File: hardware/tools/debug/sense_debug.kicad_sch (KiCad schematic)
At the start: 54 parts, among them J1 Conn_01x03_Pin, J2 Conn_01x20_Pin, J3 Conn_01x03_Pin, J4 Conn_01x15_Pin, J5 Conn_01x12_Pin, J6 B2B-PH-SM4-TB_LF__SN_, J7 Conn_01x03_Pin, Q1 Si1308EDL, U1 TMP117AIDRVR, U2 NTAG link, U3 ATtiny1626-MFR

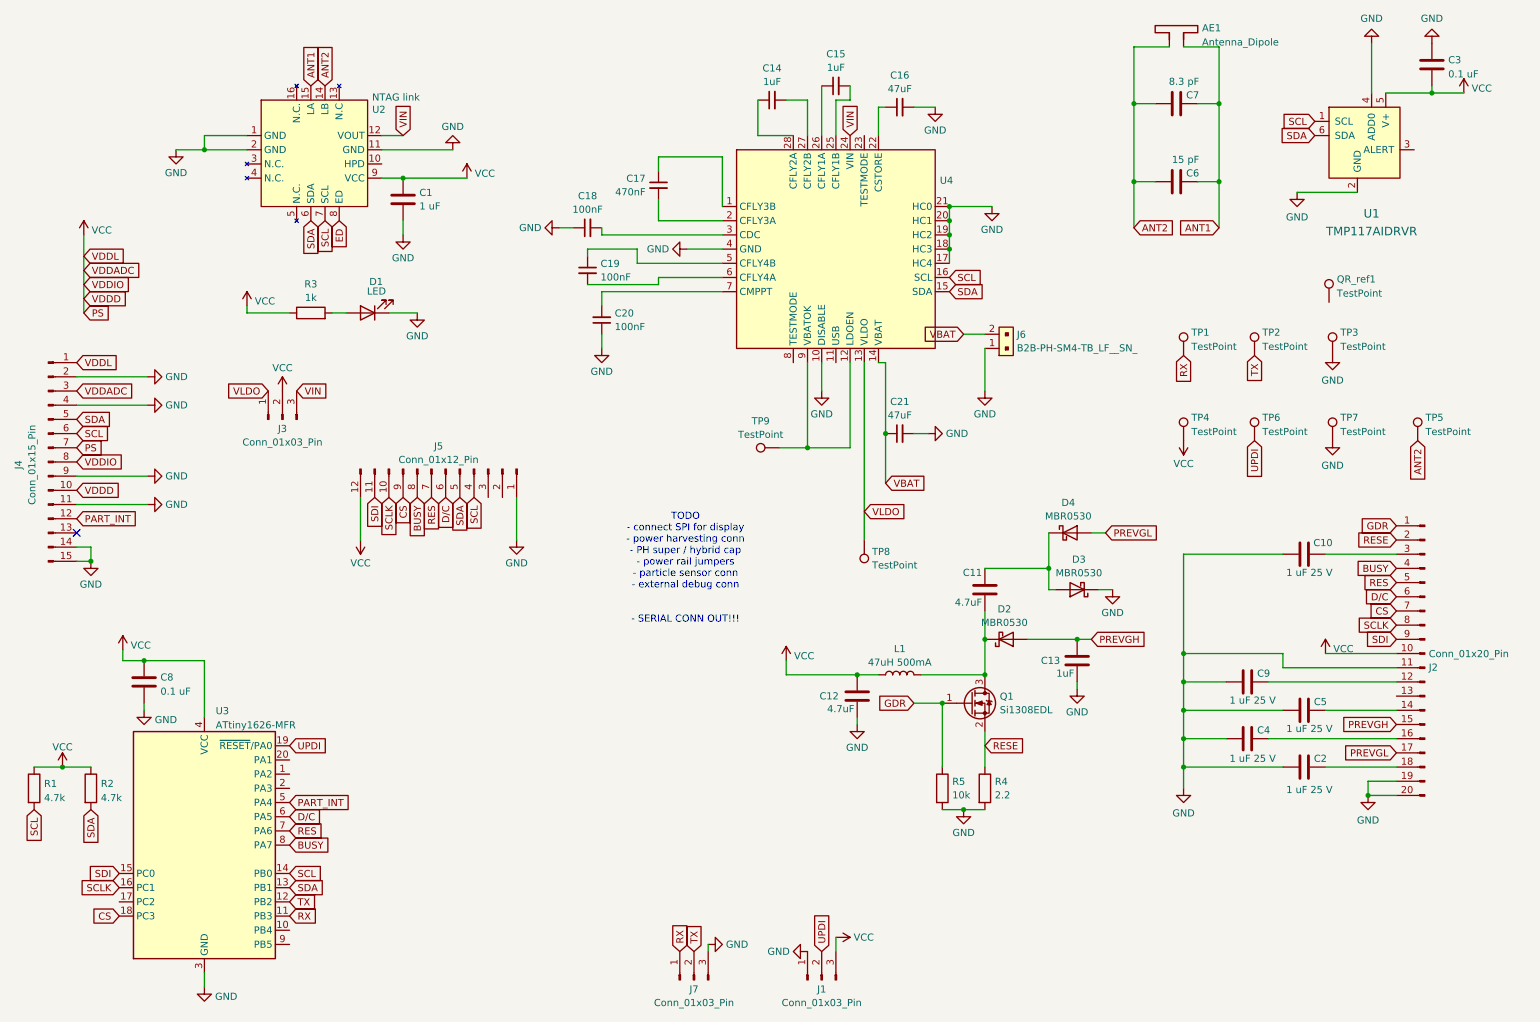
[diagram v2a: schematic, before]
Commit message: new screen debug board
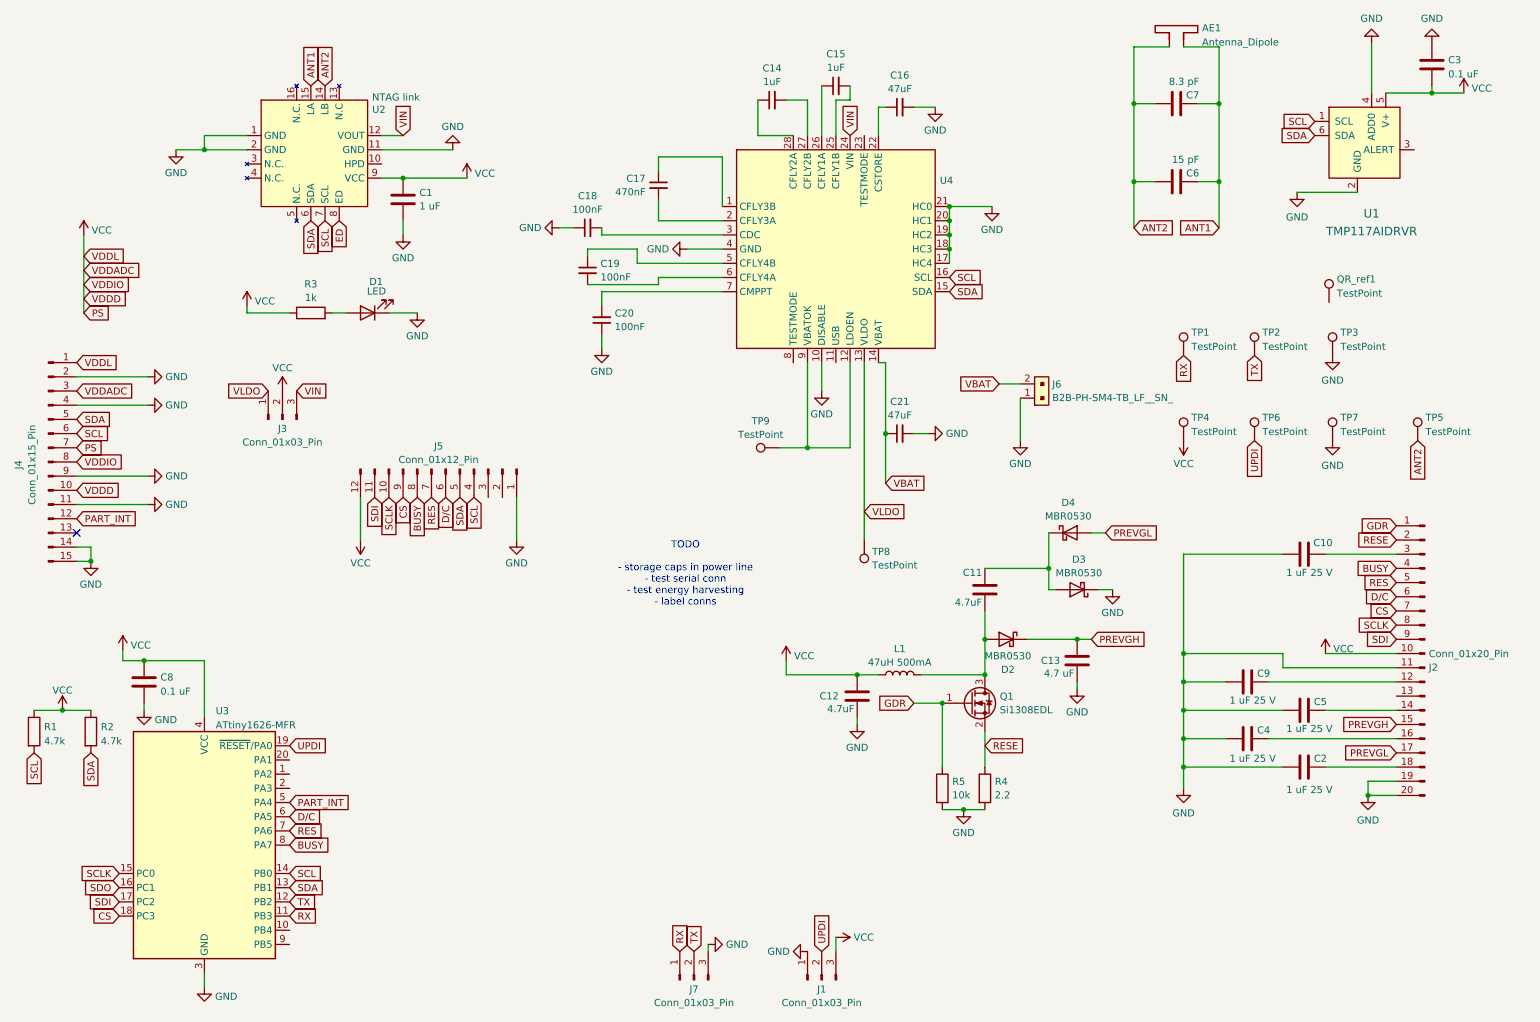
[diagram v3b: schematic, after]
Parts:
- C13: value 1uF -> 4.7 uF
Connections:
- net PREVGH: now also D2.1 (K); no longer D2.2 (A)
- net SCLK: now also U3.15 (PC0); no longer U3.16 (PC1)
- net SDI: now also U3.17 (PC2); no longer U3.15 (PC0)
- net at C11.1, L1.2, Q1.3 (D): now also D2.2 (A); no longer D2.1 (K)
- new net SDO: U3.16 (PC1)
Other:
- note added: "TODO - storage caps in power line - test serial conn - test energy harvesting - label conns"
- note removed: "TODO - connect SPI for display - power harvesting conn - PH super / hybrid cap - power rail jumpers - particle sensor conn - external debug conn - SERIAL CONN OUT!!!"
- moved on the sheet: J6, R1, R2
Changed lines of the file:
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@@
 	)
 	(junction
-		(at 22.86 149.86)
+		(at 22.86 139.7)
 		(diameter 0)
 		(color 0 0 0 0)
@@
 	(wire
 		(pts
-			(xy 17.78 149.86) (xy 22.86 149.86)
+			(xy 17.78 139.7) (xy 22.86 139.7)
 		)
 		(stroke
@@
 	(wire
 		(pts
-			(xy 184.15 72.39) (xy 187.96 72.39)
+			(xy 190.5 81.28) (xy 194.31 81.28)
 		)
 		(stroke
@@
 	(wire
 		(pts
-			(xy 22.86 149.86) (xy 27.94 149.86)
+			(xy 22.86 139.7) (xy 27.94 139.7)
 		)
 		(stroke
@@
 	(wire
 		(pts
-			(xy 187.96 74.93) (xy 187.96 82.55)
+			(xy 194.31 83.82) (xy 194.31 91.44)
 		)
 		(stroke
@@
 		)
 	)
-	(text "TODO\n- connect SPI for display\n- power harvesting conn\n- PH super / hybrid cap\n- power rail jumpers\n- particle sensor conn\n- external debug conn\n\n\n- SERIAL CONN OUT!!!\n\n"
+	(text "TODO\n\n- storage caps in power line\n- test serial conn\n- test energy harvesting\n- label conns"
 		(exclude_from_sim no)
 		(at 134.366 115.316 0)
@@
 	(global_label "VBAT"
 		(shape input)
-		(at 184.15 72.39 180)
+		(at 190.5 81.28 180)
 		(fields_autoplaced yes)
 		(effects
@@
 		)
 		(property "Intersheetrefs" "${INTERSHEET_REFS}"
-			(at 176.75 72.39 0)
+			(at 183.1 81.28 0)
 			(effects
 				(font
@@
 	(global_label "SDI"
 		(shape input)
-		(at 33.02 168.91 180)
+		(at 33.02 173.99 180)
 		(fields_autoplaced yes)
 		(effects
@@
 		)
 		(property "Intersheetrefs" "${INTERSHEET_REFS}"
-			(at 26.9505 168.91 0)
+			(at 26.9505 173.99 0)
 			(effects
 				(font
@@
 	(global_label "SDA"
 		(shape input)
-		(at 27.94 157.48 270)
+		(at 27.94 147.32 270)
 		(fields_autoplaced yes)
 		(effects
@@
 		)
 		(property "Intersheetrefs" "${INTERSHEET_REFS}"
-			(at 28.0194 163.4612 90)
+			(at 28.0194 153.3012 90)
 			(effects
 				(font
@@
 	(global_label "SCLK"
 		(shape input)
-		(at 33.02 171.45 180)
+		(at 33.02 168.91 180)
 		(fields_autoplaced yes)
 		(effects
@@
 		)
 		(property "Intersheetrefs" "${INTERSHEET_REFS}"
-			(at 25.2572 171.45 0)
+			(at 25.2572 168.91 0)
 			(effects
 				(font
@@
 	(global_label "SCL"
 		(shape input)
-		(at 17.78 157.48 270)
+		(at 17.78 147.32 270)
 		(fields_autoplaced yes)
 		(effects
@@
 		)
 		(property "Intersheetrefs" "${INTERSHEET_REFS}"
-			(at 17.8594 163.4007 90)
+			(at 17.8594 153.2407 90)
 			(effects
 				(font
@@
 		)
 	)
+	(global_label "SDO"
+		(shape input)
+		(at 33.02 171.45 180)
+		(fields_autoplaced yes)
+		(effects
+			(font
+				(size 1.27 1.27)
+			)
+			(justify right)
+		)
+		(property "Intersheetrefs" "${INTERSHEET_REFS}"
+			(at 26.2248 171.45 0)
+			(effects
+				(font
+					(size 1.27 1.27)
+				)
+				(justify right)
+				(hide yes)
+			)
+		)
+	)
 	(global_label "VDDL"
 		(shape input)
@@
 			)
 		)
-		(property "Value" "1uF"
+		(property "Value" "4.7 uF"
 			(at 203.962 133.096 0)
 			(effects
@@
 	(symbol
 		(lib_id "dk_Rectangular-Connectors-Headers-Male-Pins:B2B-PH-SM4-TB_LF__SN_")
-		(at 190.5 74.93 90)
+		(at 196.85 83.82 90)
 		(unit 1)
 		(exclude_from_sim no)
@@
 		(fields_autoplaced yes)
 		(property "Reference" "J6"
-			(at 193.675 72.4478 90)
+			(at 200.025 81.3378 90)
 			(effects
 				(font
@@
 		)
 		(property "Value" "B2B-PH-SM4-TB_LF__SN_"
-			(at 193.675 74.8721 90)
+			(at 200.025 83.7621 90)
 			(effects
 				(font
@@
 		)
 		(property "Footprint" "unsurv_offline_pcb_footprints:solar_2conn_solder"
-			(at 185.42 69.85 0)
+			(at 191.77 78.74 0)
 			(effects
 				(font
@@
 		)
 		(property "Datasheet" "http://www.jst-mfg.com/product/pdf/eng/ePH.pdf"
-			(at 182.88 69.85 0)
+			(at 189.23 78.74 0)
 			(effects
 				(font
@@
 		)
 		(property "Description" "CONN HEADER SMD 2POS 2MM"
-			(at 190.5 74.93 0)
+			(at 196.85 83.82 0)
 			(effects
 				(font
@@
 		)
 		(property "Digi-Key_PN" "455-1734-1-ND"
-			(at 180.34 69.85 0)
+			(at 186.69 78.74 0)
 			(effects
 				(font
@@
 		)
 		(property "MPN" "B2B-PH-SM4-TB(LF)(SN)"
-			(at 177.8 69.85 0)
+			(at 184.15 78.74 0)
 			(effects
 				(font
@@
 		)
 		(property "Category" "Connectors, Interconnects"
-			(at 175.26 69.85 0)
+			(at 181.61 78.74 0)
 			(effects
 				(font
@@
 		)
 		(property "Family" "Rectangular Connectors - Headers, Male Pins"
-			(at 172.72 69.85 0)
+			(at 179.07 78.74 0)
 			(effects
 				(font
@@
 		)
 		(property "DK_Datasheet_Link" "http://www.jst-mfg.com/product/pdf/eng/ePH.pdf"
-			(at 170.18 69.85 0)
+			(at 176.53 78.74 0)
 			(effects
 				(font
@@
 		)
 		(property "DK_Detail_Page" "/product-detail/en/jst-sales-america-inc/B2B-PH-SM4-TB(LF)(SN)/455-1734-1-ND/926831"
-			(at 167.64 69.85 0)
+			(at 173.99 78.74 0)
 			(effects
 				(font
@@
 		)
 		(property "Description_1" "CONN HEADER SMD 2POS 2MM"
-			(at 165.1 69.85 0)
+			(at 171.45 78.74 0)
 			(effects
 				(font
@@
 		)
 		(property "Manufacturer" "JST Sales America Inc."
-			(at 162.56 69.85 0)
+			(at 168.91 78.74 0)
 			(effects
 				(font
@@
 		)
 		(property "Status" "Active"
-			(at 160.02 69.85 0)
+			(at 166.37 78.74 0)
 			(effects
 				(font
@@
 	(symbol
 		(lib_id "Device:R")
-		(at 27.94 153.67 0)
+		(at 27.94 143.51 0)
 		(unit 1)
 		(exclude_from_sim no)
@@
 		(fields_autoplaced yes)
 		(property "Reference" "R2"
-			(at 29.718 152.8353 0)
+			(at 29.718 142.6753 0)
 			(effects
 				(font
@@
 		)
 		(property "Value" "4.7k"
-			(at 29.718 155.3722 0)
+			(at 29.718 145.2122 0)
 			(effects
 				(font
@@
 		)
 		(property "Footprint" "Resistor_SMD:R_0603_1608Metric"
-			(at 26.162 153.67 90)
+			(at 26.162 143.51 90)
 			(effects
 				(font
@@
 		)
 		(property "Datasheet" "~"
-			(at 27.94 153.67 0)
+			(at 27.94 143.51 0)
 			(effects
 				(font
@@
 		)
 		(property "Description" ""
-			(at 27.94 153.67 0)
+			(at 27.94 143.51 0)
 			(effects
 				(font
@@
 	(symbol
 		(lib_id "power:GND")
-		(at 187.96 82.55 0)
+		(at 194.31 91.44 0)
 		(unit 1)
 		(exclude_from_sim no)
@@
 		(fields_autoplaced yes)
 		(property "Reference" "#PWR036"
-			(at 187.96 88.9 0)
+			(at 194.31 97.79 0)
 			(effects
 				(font
@@
 		)
 		(property "Value" "GND"
-			(at 187.96 86.6831 0)
+			(at 194.31 95.5731 0)
 			(effects
 				(font
@@
 		)
 		(property "Footprint" ""
-			(at 187.96 82.55 0)
+			(at 194.31 91.44 0)
 			(effects
 				(font
@@
 		)
 		(property "Datasheet" ""
-			(at 187.96 82.55 0)
+			(at 194.31 91.44 0)
 			(effects
 				(font
@@
 		)
 		(property "Description" ""
-			(at 187.96 82.55 0)
+			(at 194.31 91.44 0)
 			(effects
 				(font
@@
 	(symbol
 		(lib_id "power:VCC")
-		(at 22.86 149.86 0)
+		(at 22.86 139.7 0)
 		(unit 1)
 		(exclude_from_sim no)
@@
 		(fields_autoplaced yes)
 		(property "Reference" "#PWR017"
-			(at 22.86 153.67 0)
+			(at 22.86 143.51 0)
 			(effects
 				(font
@@
 		)
 		(property "Value" "VCC"
-			(at 22.86 146.2842 0)
+			(at 22.86 136.1242 0)
 			(effects
 				(font
@@
 		)
 		(property "Footprint" ""
-			(at 22.86 149.86 0)
+			(at 22.86 139.7 0)
 			(effects
 				(font
@@
 		)
 		(property "Datasheet" ""
-			(at 22.86 149.86 0)
+			(at 22.86 139.7 0)
 			(effects
 				(font
@@
 		)
 		(property "Description" ""
-			(at 22.86 149.86 0)
+			(at 22.86 139.7 0)
 			(effects
 				(font
@@
 	(symbol
 		(lib_id "Device:R")
-		(at 17.78 153.67 0)
+		(at 17.78 143.51 0)
 		(unit 1)
 		(exclude_from_sim no)
@@
 		(fields_autoplaced yes)
 		(property "Reference" "R1"
-			(at 19.558 152.8353 0)
+			(at 19.558 142.6753 0)
 			(effects
 				(font
@@
 		)
 		(property "Value" "4.7k"
-			(at 19.558 155.3722 0)
+			(at 19.558 145.2122 0)
 			(effects
 				(font
@@
 		)
 		(property "Footprint" "Resistor_SMD:R_0603_1608Metric"
-			(at 16.002 153.67 90)
+			(at 16.002 143.51 90)
 			(effects
 				(font
@@
 		)
 		(property "Datasheet" "~"
-			(at 17.78 153.67 0)
+			(at 17.78 143.51 0)
 			(effects
 				(font
@@
 		)
 		(property "Description" ""
-			(at 17.78 153.67 0)
+			(at 17.78 143.51 0)
 			(effects
 				(font
@@
 		(lib_id "Diode:MBR0530")
 		(at 191.77 127 0)
-		(mirror x)
+		(mirror y)
 		(unit 1)
 		(exclude_from_sim no)
@@
 		(dnp no)
 		(property "Reference" "D2"
-			(at 191.4525 121.5855 0)
+			(at 192.0875 132.4145 0)
 			(effects
 				(font
@@
 		)
 		(property "Value" "MBR0530"
-			(at 191.4525 124.0098 0)
+			(at 192.0875 129.9902 0)
 			(effects
 				(font
@@
 		)
 		(property "Footprint" "Diode_SMD:D_SOD-123"
-			(at 191.77 122.555 0)
+			(at 191.77 131.445 0)
 			(effects
 				(font

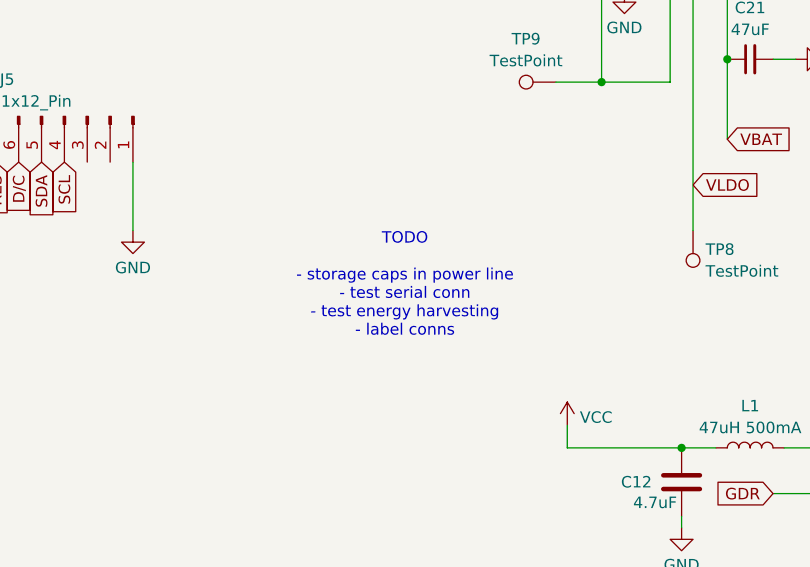
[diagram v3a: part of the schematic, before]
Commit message: update SDO SDI SCLK
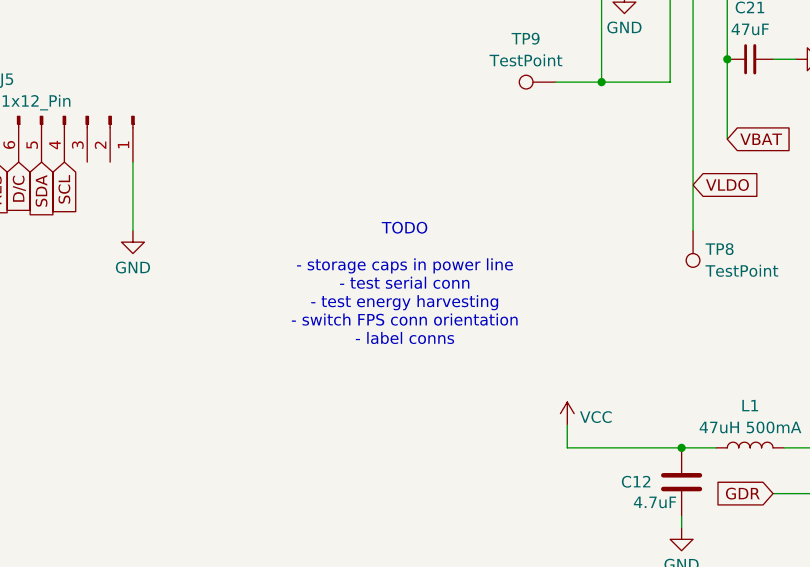
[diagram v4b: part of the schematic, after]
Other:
- note added: "TODO - storage caps in power line - test serial conn - test energy harvesting - switch FPS conn orientation - label conns"
- note removed: "TODO - storage caps in power line - test serial conn - test energy harvesting - label conns"
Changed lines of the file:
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@@
 		)
 	)
-	(text "TODO\n\n- storage caps in power line\n- test serial conn\n- test energy harvesting\n- label conns"
+	(text "TODO\n\n- storage caps in power line\n- test serial conn\n- test energy harvesting\n- switch FPS conn orientation\n- label conns"
 		(exclude_from_sim no)
 		(at 134.366 115.316 0)
